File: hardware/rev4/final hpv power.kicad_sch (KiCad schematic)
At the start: 32 parts, among them J1 Conn_01x12, J2 Conn_01x04_Pin, J3 USB_C_Receptacle_USB2.0_14P, Q1 PNP, SW2 SW_SPST, U1 ESP32-S3-WROOM-1, U2 MCP1825S, U3 HX711

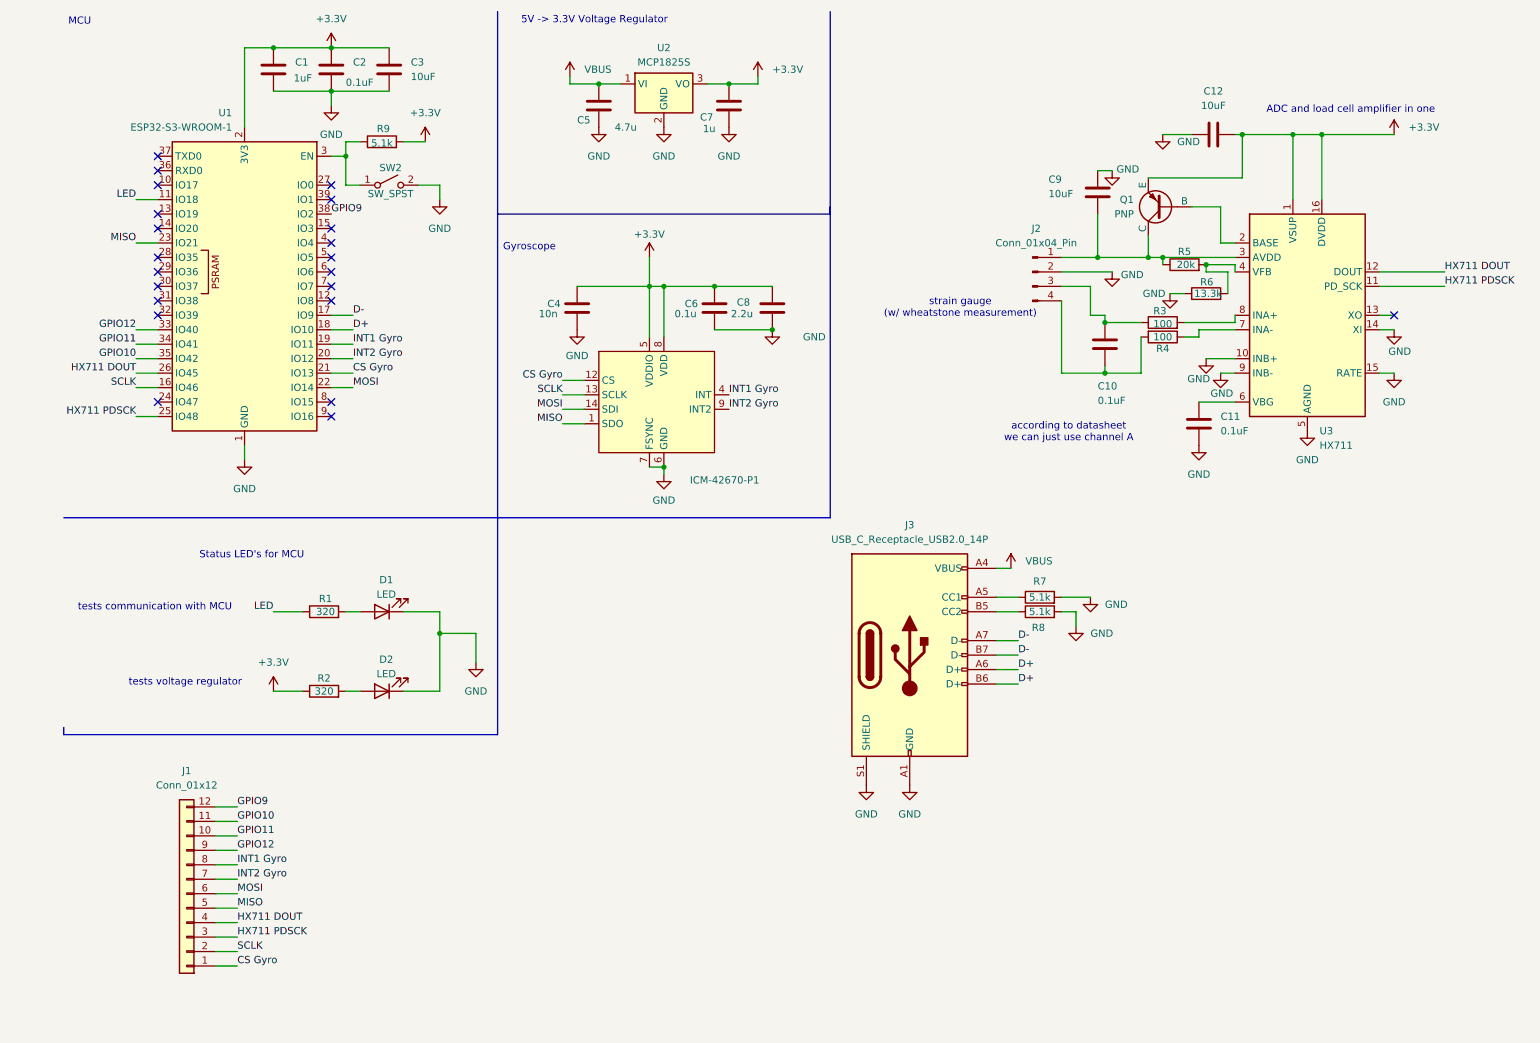
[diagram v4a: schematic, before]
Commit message: created BOM
updated symbol fields
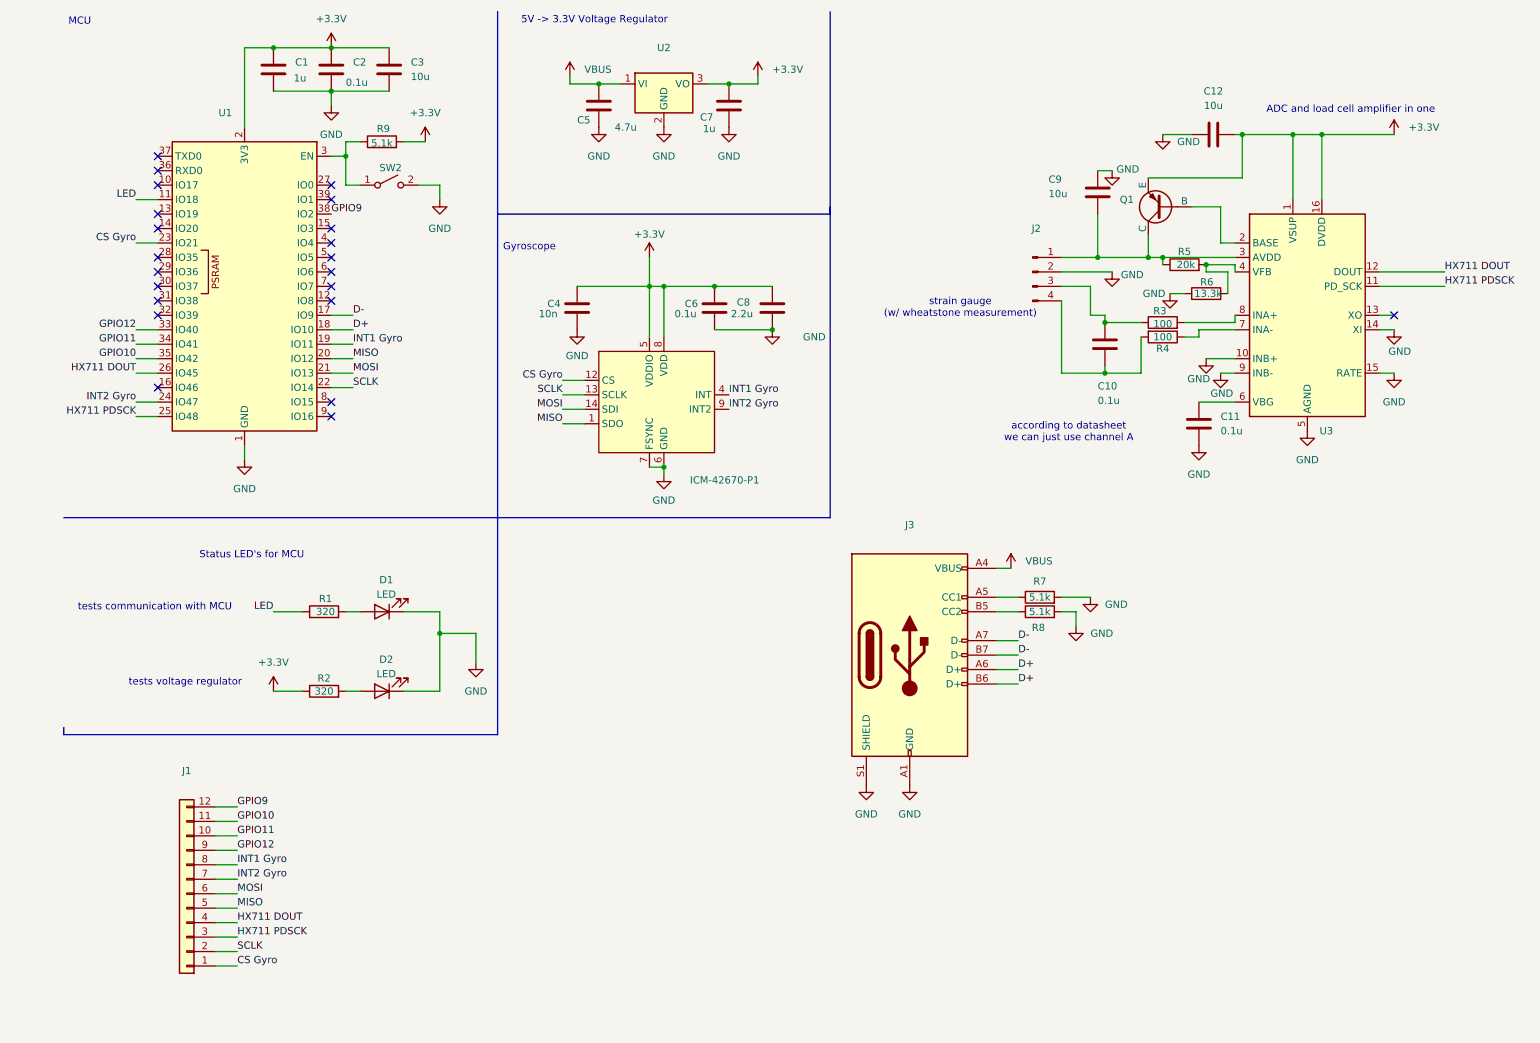
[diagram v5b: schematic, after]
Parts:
- C1: value 1uF -> 1u; Digikey Link https://www.digikey.ca/en/products/detail/samsung-electro-mechanics/CL10B105KP8NNNC/3887604 -> https://www.digikey.ca/en/products/detail/samsung-electro-mechanics/CL21B105KAFNNNE/3886724; Manufacturer (none) -> Samsung Electro-Mechanics; Part number (none) -> CL21B105KAFNNNE
- C10, C11, C2: value 0.1uF -> 0.1u; Digikey Link https://www.digikey.ca/en/products/detail/kemet/C0603C104K5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 -> https://www.digikey.ca/en/products/detail/kemet/C0805C104K5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; Manufacturer (none) -> KEMET; Part number (none) -> C0805C104K5RACTU
- C12, C3, C9: value 10uF -> 10u; Manufacturer (none) -> Samsung Electro-Mechanics; Part number (none) -> CL10A106KP8NNNC
- C4: Digikey Link https://www.digikey.ca/en/products/detail/kemet/C0603C103K5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 -> https://www.digikey.ca/en/products/detail/kemet/C0805C103K5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; Manufacturer (none) -> KEMET; Part number (none) -> C0805C103K5RACTU
- C5: Digikey Link https://www.digikey.ca/en/products/detail/samsung-electro-mechanics/CL10A475KP8NNNC/3886702 -> https://www.digikey.ca/en/products/detail/samsung-electro-mechanics/CL21A475KAQNNNE/3886902; Manufacturer (none) -> Samsung Electro-Mechanics; Part number (none) -> CL21A475KAQNNNE
- C6: Digikey Link https://www.digikey.ca/en/products/detail/kemet/C0603C104K5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 -> https://www.digikey.ca/en/products/detail/kemet/C0805C104K5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; Manufacturer (none) -> KEMET; Part number (none) -> C0805C104K5RACTU
- C7: Digikey Link https://www.digikey.ca/en/products/detail/samsung-electro-mechanics/CL10B105KP8NNNC/3887604 -> https://www.digikey.ca/en/products/detail/samsung-electro-mechanics/CL21B105KAFNNNE/3886724; Manufacturer (none) -> Samsung Electro-Mechanics; Part number (none) -> CL21B105KAFNNNE
- C8: Digikey Link https://www.digikey.ca/en/products/detail/samsung-electro-mechanics/CL10B225KP8NNNC/3886792 -> https://www.digikey.ca/en/products/detail/samsung-electro-mechanics/CL21B225KAFNNNE/3888612; Manufacturer (none) -> Samsung Electro-Mechanics; Part number (none) -> CL21B225KAFNNNE
- D1, D2: Digikey Link https://www.digikey.ca/en/products/detail/w%C3%BCrth-elektr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 -> https://www.digikey.ca/en/products/detail/liteon/LTST-C170G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; Manufacturer (none) -> Lite-On Inc.; Part number (none) -> LTST-C170GKT
- ICM-42670-P1: Digikey Link https://www.digikey.ca/en/products/detail/tdk-invensense/ICM-42670-P/14319524?s=N4IgTCBcDaIJIGECyBaALGAbAdgAwgF0BfIA -> https://www.digikey.ca/en/products/detail/tdk-invensense/ICM-42670-P/14319524?s=N4IgTCBcDaIJIGECyBaALGAbAdgAwgF0BfIA; Manufacturer (none) -> TDK InvenSense; Part number (none) -> ICM-42670-P
- J1: value Conn_01x12 -> ~; Digikey Link (none) -> https://www.digikey.ca/en/products/detail/jst-sales-america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; Item Name (none) -> Breakout header; Manufacturer (none) -> JST Sales America Inc.; Part number (none) -> B12B-XH-A
- J2: value Conn_01x04_Pin -> ~; Digikey Link https://www.digikey.ca/en/products/detail/jst-sales-america-inc/S4B-EH/926535?s=N4IgTCBcDaIFIGUAqACAxgewHZYKZoBcMAnFBAFgCEUBRACRAF0BfIA -> https://www.digikey.ca/en/products/detail/jst-sales-america-inc/B4B-XH-A/1651047; Manufacturer (none) -> JST Sales America Inc.; Part number (none) -> B4B-XH-A
- J3: value USB_C_Receptacle_USB2.0_14P -> ~; Digikey Link (none) -> https://www.digikey.ca/en/products/detail/gct/USB4110-GF-A/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; Manufacturer (none) -> GCT; Part number (none) -> USB4110-GF-A
- Q1: value PNP -> ~; Digikey Link https://www.digikey.ca/en/products/detail/mcc-micro-commercial-components/MMSS8550-L-TP/2827198 -> https://www.digikey.ca/en/products/detail/mcc-micro-commercial-components/MMSS8550-L-TP/2827198; Manufacturer (none) -> MCC (Micro Commercial Components); Part number (none) -> MMSS8550-L-TP
- R1, R2: Digikey Link https://www.digikey.ca/en/products/detail/koa-speer-electro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 -> https://www.digikey.ca/en/products/detail/yageo/RT0805BRD07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; Manufacturer (none) -> YAGEO; Part number (none) -> RT0805BRD07320RL
- R3, R4: Digikey Link https://www.digikey.ca/en/products/detail/yageo/RC0603FR-07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 -> https://www.digikey.ca/en/products/detail/vishay-dale/CRCW0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; Manufacturer (none) -> Vishay Dale; Part number (none) -> CRCW0805100RFKEA
- R5: Digikey Link https://www.digikey.ca/en/products/detail/yageo/RC0603FR-07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 -> https://www.digikey.ca/en/products/detail/panasonic-electro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; Manufacturer (none) -> Panasonic Electronic Components; Part number (none) -> ERA-6AEB203V
- R6: Digikey Link https://www.digikey.ca/en/products/detail/stackpole-electro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 -> https://www.digikey.ca/en/products/detail/vishay-dale/CRCW0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; Manufacturer (none) -> Vishay Dale; Part number (none) -> CRCW080513K3FKEA
- R7, R8, R9: Digikey Link (none) -> https://www.digikey.ca/en/products/detail/stackpole-electro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; Manufacturer (none) -> Stackpole Electronics Inc; Part number (none) -> RMCF0805JT5K10
- SW2: value SW_SPST -> ~; Digikey Link (none) -> https://www.digikey.ca/en/products/detail/schurter-inc/1301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; Item Name (none) -> Enable switch; Manufacturer (none) -> SCHURTER Inc.; Part number (none) -> 1301.9314.24
- U1: value ESP32-S3-WROOM-1 -> ~; Digikey Link https://www.digikey.ca/en/products/detail/espressif-systems/ESP32-S3-WROOM-1-N4R2/16162643 -> https://www.digikey.ca/en/products/detail/espressif-systems/ESP32-S3-WROOM-1-N4R2/16162643; Manufacturer (none) -> Espressif Systems; Part number (none) -> ESP32-S3-WROOM-1-N4R2
- U2: value MCP1825S -> ~; Manufacturer (none) -> Microchip Technology; Part number (none) -> MCP1825ST-3302E/DB
- U3: value HX711 -> ~; Manufacturer (none) -> SparkFun Electronics; Part number (none) -> 13879
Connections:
- net CS Gyro: now also U1.23 (IO21); no longer U1.21 (IO13)
- net INT2 Gyro: now also U1.24 (IO47); no longer U1.20 (IO12)
- net MISO: now also U1.20 (IO12); no longer U1.23 (IO21)
- net MOSI: now also U1.21 (IO13); no longer U1.22 (IO14)
- net SCLK: now also U1.22 (IO14); no longer U1.16 (IO46)

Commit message: connected TX and RX pins on MCU to header
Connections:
- net GPIO11 is gone; now on net GPIO9: J1.10 (Pin_10), U1.34 (IO41)
- net GPIO12 is gone; now on net GPIO10: J1.9 (Pin_9), U1.33 (IO40)
- net GPIO10: no longer J1.11 (Pin_11), U1.35 (IO42)
- net GPIO9: no longer J1.12 (Pin_12), U1.38 (IO2)
- net RX: now reaches U1.36 (RXD0)
- net RX: now also J1.11 (Pin_11)
- net TX: now reaches U1.37 (TXD0)
- net TX: now also J1.12 (Pin_12)
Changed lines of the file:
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@@
 	)
 	(no_connect
-		(at 40.64 43.18)
+		(at 40.64 76.2)
+	)
+	(no_connect
+		(at 71.12 50.8)
 	)
 	(no_connect
@@
 		(at 71.12 63.5)
 	)
-	(no_connect
-		(at 40.64 40.64)
-	)
-	(wire
-		(pts
-			(xy 36.83 76.2) (xy 40.64 76.2)
-		)
-		(stroke
-			(width 0)
-			(type default)
-		)
-	)
 	(wire
 		(pts
@@
 	(wire
 		(pts
+			(xy 36.83 43.18) (xy 40.64 43.18)
+		)
+		(stroke
+			(width 0)
+			(type default)
+		)
+	)
+	(wire
+		(pts
 			(xy 217.17 58.42) (xy 217.17 59.69)
 		)
@@
 	(wire
 		(pts
+			(xy 36.83 40.64) (xy 40.64 40.64)
+		)
+		(stroke
+			(width 0)
+			(type default)
+		)
+	)
+	(wire
+		(pts
 			(xy 118.11 27.94) (xy 121.92 27.94)
 		)
@@
 			(width 0)
 			(type default)
-		)
-	)
-	(label "GPIO11"
-		(at 36.83 73.66 180)
-		(effects
-			(font
-				(size 1.27 1.27)
-			)
-			(justify right bottom)
-		)
-	)
-	(label "GPIO10"
-		(at 54.61 157.48 0)
-		(effects
-			(font
-				(size 1.27 1.27)
-			)
-			(justify left bottom)
 		)
 	)
@@
 		)
 	)
-	(label "GPIO9"
-		(at 54.61 154.94 0)
-		(effects
-			(font
-				(size 1.27 1.27)
-			)
-			(justify left bottom)
+	(label "GPIO10"
+		(at 36.83 71.12 180)
+		(effects
+			(font
+				(size 1.27 1.27)
+			)
+			(justify right bottom)
 		)
 	)
@@
 		)
 	)
+	(label "TX"
+		(at 36.83 40.64 180)
+		(effects
+			(font
+				(size 1.27 1.27)
+			)
+			(justify right bottom)
+		)
+	)
+	(label "RX"
+		(at 36.83 43.18 180)
+		(effects
+			(font
+				(size 1.27 1.27)
+			)
+			(justify right bottom)
+		)
+	)
 	(label "D-"
 		(at 191.77 128.27 0)
@@
 		)
 	)
-	(label "GPIO12"
-		(at 36.83 71.12 180)
-		(effects
-			(font
-				(size 1.27 1.27)
-			)
-			(justify right bottom)
-		)
-	)
 	(label "INT1 Gyro"
 		(at 140.97 82.55 0)
@@
 		)
 	)
+	(label "TX"
+		(at 54.61 154.94 0)
+		(effects
+			(font
+				(size 1.27 1.27)
+			)
+			(justify left bottom)
+		)
+	)
 	(label "LED"
 		(at 36.83 48.26 180)
@@
 		)
 	)
+	(label "GPIO9"
+		(at 54.61 160.02 0)
+		(effects
+			(font
+				(size 1.27 1.27)
+			)
+			(justify left bottom)
+		)
+	)
 	(label "HX711 PDSCK"
 		(at 54.61 177.8 0)
@@
 		)
 	)
-	(label "GPIO12"
-		(at 54.61 162.56 0)
-		(effects
-			(font
-				(size 1.27 1.27)
-			)
-			(justify left bottom)
-		)
-	)
 	(label "INT2 Gyro"
 		(at 54.61 167.64 0)
@@
 		)
 	)
-	(label "GPIO11"
-		(at 54.61 160.02 0)
-		(effects
-			(font
-				(size 1.27 1.27)
-			)
-			(justify left bottom)
-		)
-	)
 	(label "MOSI"
 		(at 111.76 85.09 180)
@@
 		)
 	)
+	(label "GPIO9"
+		(at 36.83 73.66 180)
+		(effects
+			(font
+				(size 1.27 1.27)
+			)
+			(justify right bottom)
+		)
+	)
 	(label "MISO"
 		(at 111.76 87.63 180)
@@
 		)
 	)
-	(label "GPIO9"
-		(at 71.12 50.8 0)
+	(label "RX"
+		(at 54.61 157.48 0)
+		(effects
+			(font
+				(size 1.27 1.27)
+			)
+			(justify left bottom)
+		)
+	)
+	(label "GPIO10"
+		(at 54.61 162.56 0)
 		(effects
 			(font
@@
 		)
 	)
-	(label "GPIO10"
-		(at 36.83 76.2 180)
-		(effects
-			(font
-				(size 1.27 1.27)
-			)
-			(justify right bottom)
-		)
-	)
